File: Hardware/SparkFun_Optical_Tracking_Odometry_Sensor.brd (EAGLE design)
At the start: 25.4 x 25.4 mm, 78 parts, among them J1 QWIIC_RIGHT_ANGLE, J2 QWIIC_RIGHT_ANGLE, Q1 100mA/20V/3.8Ω, Q2 100mA/20V/3.8Ω, U1 PAA5160E1-Q, U2 LSM6DS0, U3 STM32C011F6U6, U4 RT9080-18GJ5

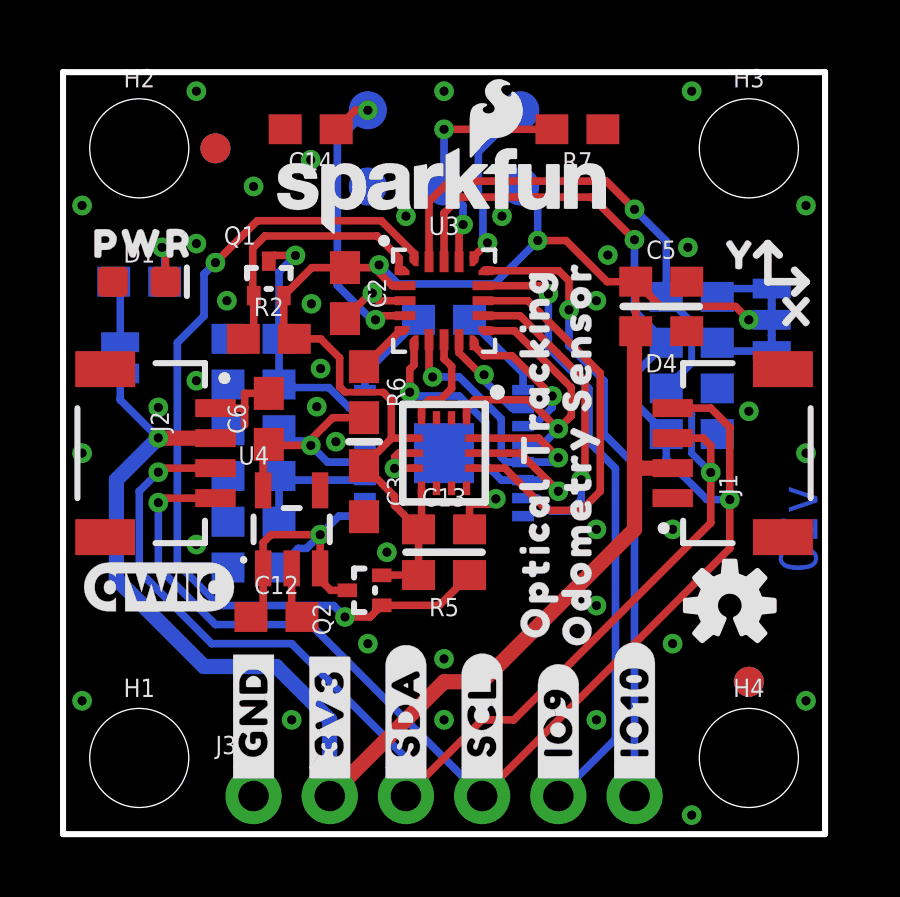
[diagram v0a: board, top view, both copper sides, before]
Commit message: v11 updates
Bump version number to v11
Fix PAA5160 footprint (pad pitch was 0.6mm instead of 0.65mm, and needed to be pushed out 0.1mm)
Fix power LED orientation (doh!)
Fix measures
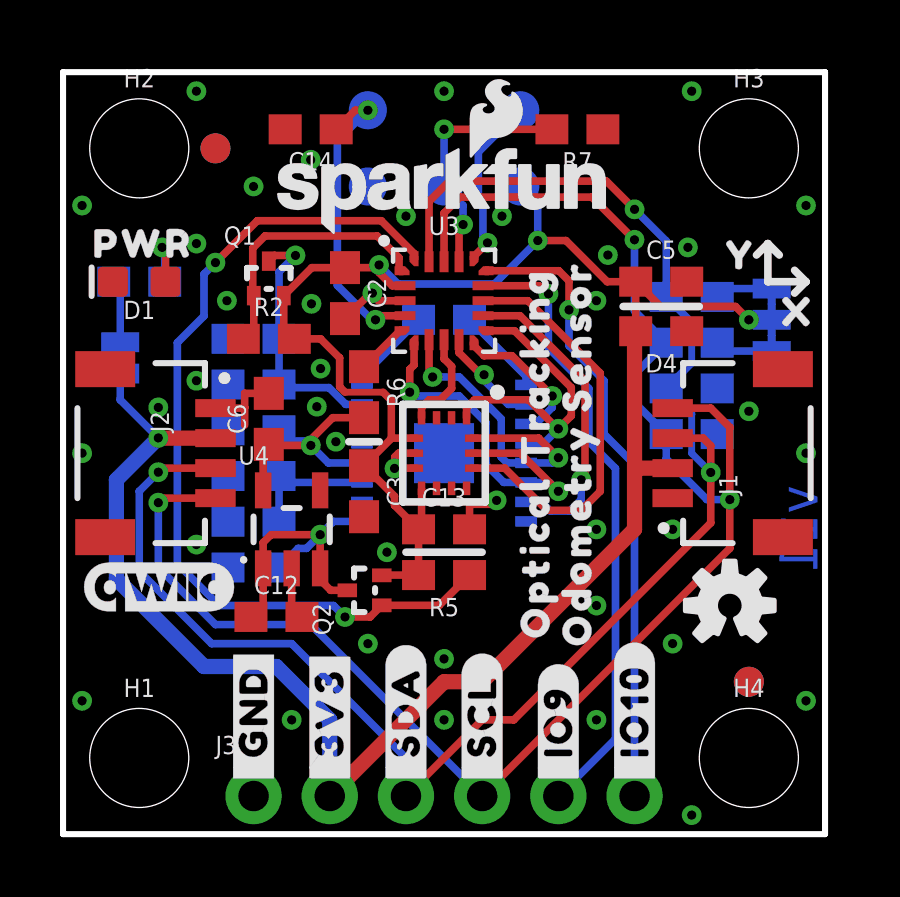
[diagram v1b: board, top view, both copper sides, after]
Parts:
- turned D1 to 180 degrees
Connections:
- net GND: now also D1.C; no longer D1.A
- net N$2: now also D1.A; no longer D1.C
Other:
- board text added: "v11"
- board text removed: "v10"
